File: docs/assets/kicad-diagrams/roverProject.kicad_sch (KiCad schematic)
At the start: 4 parts, among them M1 DC Motor w/ Encoder, M2 DC Motor w/ Encoder

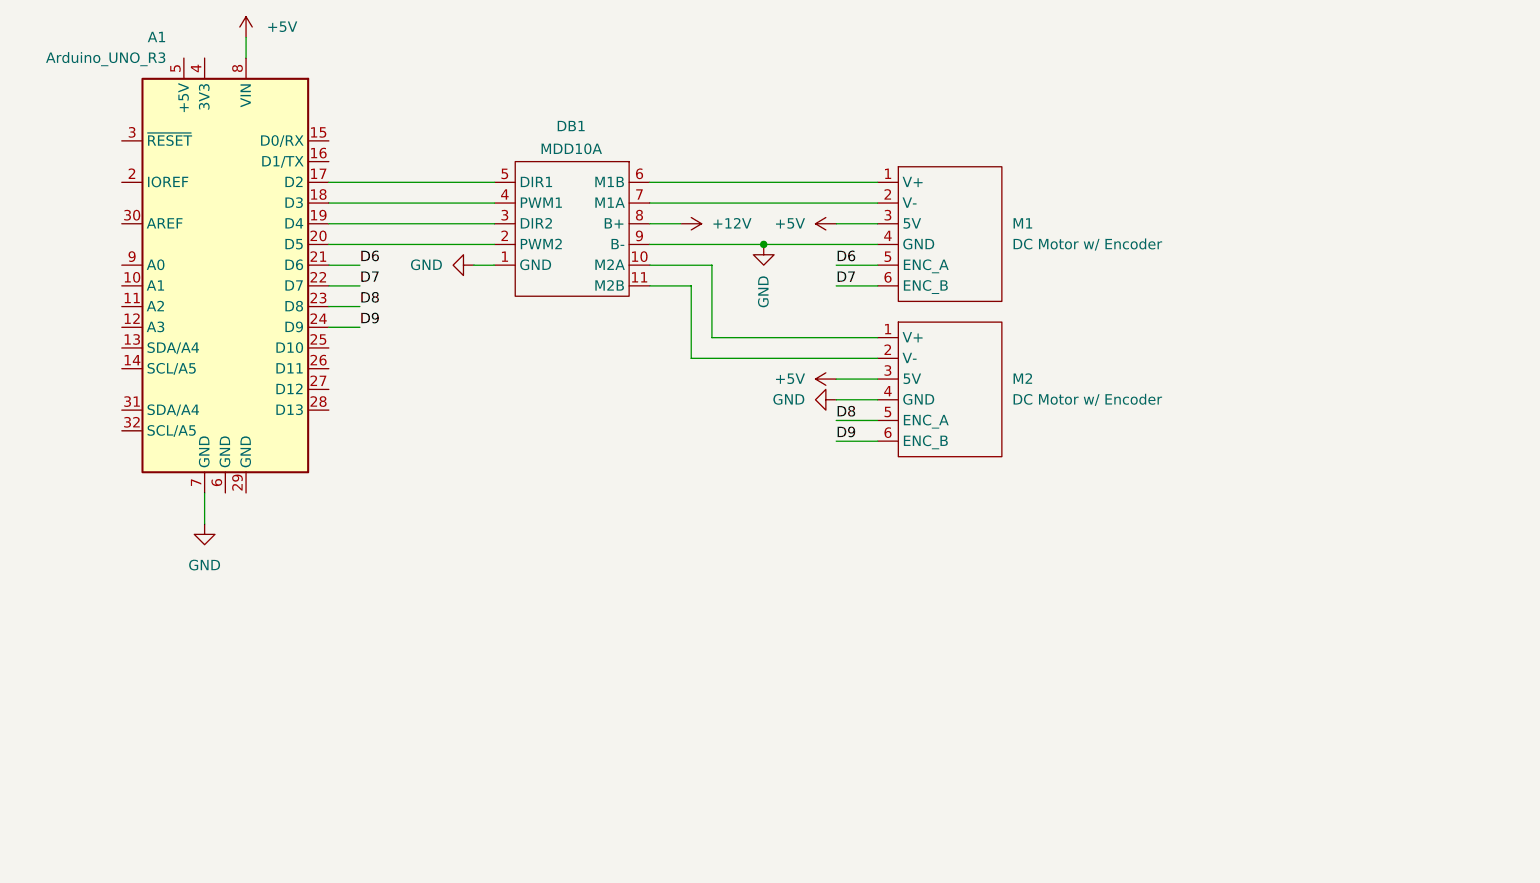
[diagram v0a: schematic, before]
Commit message: Update /kicad-diagrams
Updated /kicad-diagrams with more components
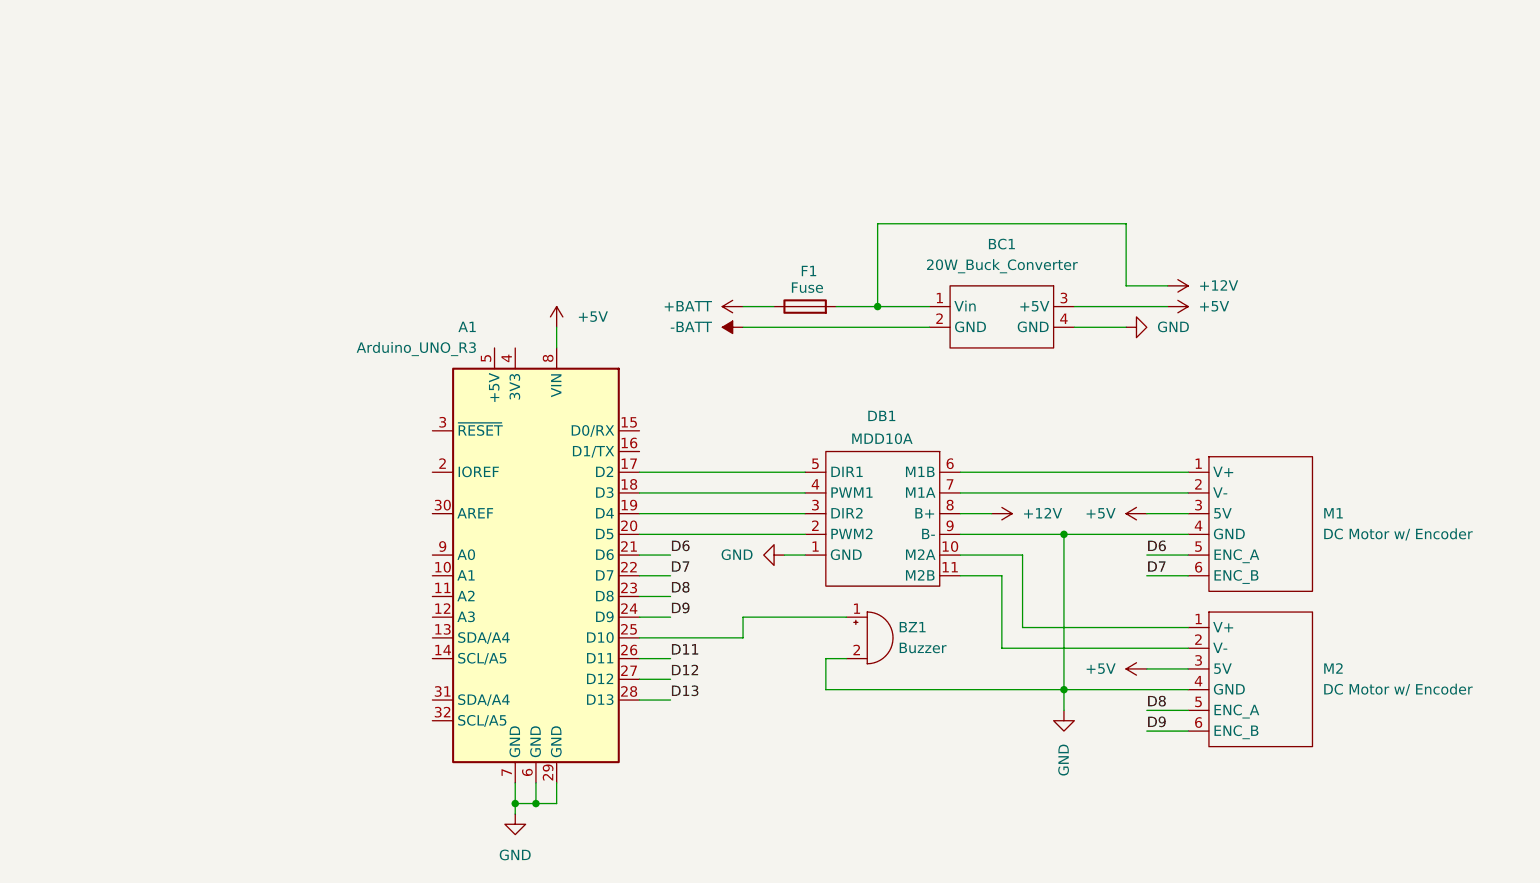
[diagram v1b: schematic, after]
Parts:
- added BC1: 20W_Buck_Converter, symbol roverProjectLib:20W_Buck_Converter
- added BZ1: Buzzer, symbol Device:Buzzer
- added F1: Fuse, symbol Device:Fuse
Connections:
- net +12V: now also BC1.1 (Vin), F1.2
- net +5V: now also BC1.3 (+5V)
- net GND: now also A1.29 (GND), A1.6 (GND), BC1.4 (GND), BZ1.2 (-)
- net at A1.25 (D10): now also BZ1.1 (+)
- net D11: now reaches A1.26 (D11)
- net D12: now reaches A1.27 (D12)
- net D13: now reaches A1.28 (D13)
- new net +BATT: F1.1
- new net -BATT: BC1.2 (GND)
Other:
- title: (none) -> Rover Project
- moved on the sheet: A1, DB1, M1, M2
